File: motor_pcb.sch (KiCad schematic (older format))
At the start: 37 parts, among them J1 Screw_Terminal_01x02, J2 Screw_Terminal_01x02, J3 Conn_01x04, J4 Conn_01x04, J5 Screw_Terminal_01x04, J6 Screw_Terminal_01x04, J7 Conn_01x04, J8 Conn_01x04, U2 A-Star_328PB_Micro, U3 DRV8834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

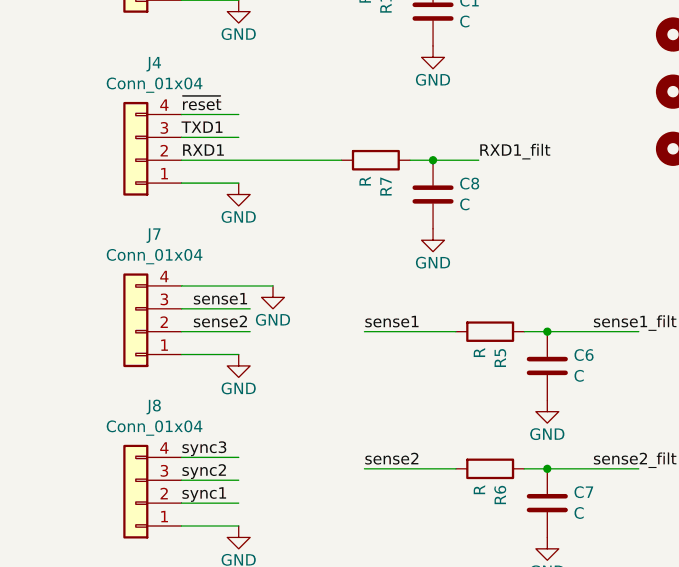
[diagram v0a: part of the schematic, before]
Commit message: added 5V to sensor connector
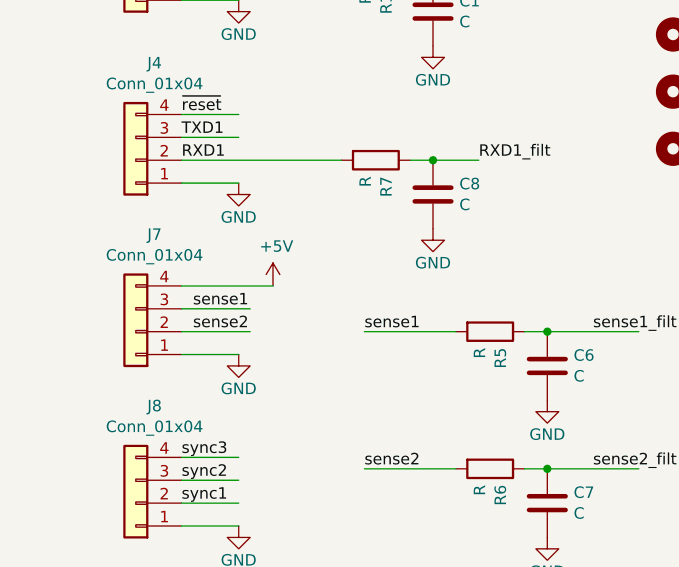
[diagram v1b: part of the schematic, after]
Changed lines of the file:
@@
 	2700 2100 3200 2100
 $Comp
-L power:GND #PWR?
-U 1 1 5E10BB71
+L power:+5V #PWR?
+U 1 1 5DD53D73
 P 2050 4600
-F 0 "#PWR?" H 2050 4350 50  0001 C CNN
-F 1 "GND" H 2050 4450 50  0000 C CNN
+F 0 "#PWR?" H 2050 4450 50  0001 C CNN
+F 1 "+5V" H 2065 4773 50  0000 C CNN
 F 2 "" H 2050 4600 50  0001 C CNN
 F 3 "" H 2050 4600 50  0001 C CNN

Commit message: updated with previously uncommitted changes. Added schematics
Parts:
- R2: value R -> 5.6k
- R3: value R -> 1k
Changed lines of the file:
@@
 P 4850 2350
 F 0 "R3" H 4920 2396 50  0000 L CNN
-F 1 "R" H 4920 2305 50  0000 L CNN
+F 1 "1k" H 4920 2305 50  0000 L CNN
 F 2 "Resistor_SMD:R_0603_1608Metric" V 4780 2350 50  0001 C CNN
 F 3 "~" H 4850 2350 50  0001 C CNN
@@
 P 4400 2650
 F 0 "R2" H 4470 2696 50  0000 L CNN
-F 1 "R" H 4470 2605 50  0000 L CNN
+F 1 "5.6k" H 4470 2605 50  0000 L CNN
 F 2 "Resistor_SMD:R_0603_1608Metric" V 4330 2650 50  0001 C CNN
 F 3 "~" H 4400 2650 50  0001 C CNN
